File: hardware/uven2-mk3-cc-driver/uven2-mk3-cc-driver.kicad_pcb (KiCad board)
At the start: 2 copper layers, 80 x 32 mm, 23 parts, among them J1 Conn_01x03_Pin, J2 ADJ, J3 current_measurement, Q1 AO3401A, U2 LM3409HV

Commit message: ordered
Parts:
- removed D3: SS34, custom_lib:DIO_SS34
- added D1: SS54-HF, custom_lib:DIOM5025X220N, F.Cu at (126.0, 87.9)
- C1: value 3.3µF -> 16SVP3R3M; footprint Capacitor_SMD:C_Elec_5x5.4 -> custom_lib:CAP_16SVP3R3M
- L1: footprint Inductor_SMD:L_7.3x7.3_H3.5 -> custom_lib:HPC-8040NV-100M
- R1, R2, R3: footprint Resistor_SMD:R_0805_2012Metric_Pad1.20x1.40mm_HandSolder -> Resistor_SMD:R_0603_1608Metric_Pad0.98x0.95mm_HandSolder
- R4: footprint Resistor_SMD:R_0805_2012Metric_Pad1.20x1.40mm_HandSolder -> Resistor_SMD:R_2512_6332Metric_Pad1.40x3.35mm_HandSolder
- moved R1 5.09 mm to (115.1, 89.9), turned to 180 degrees
- moved C1 5.00 mm to (111.0, 103.4)
- moved R2 4.20 mm to (110.8, 89.9), turned to 180 degrees
- moved R4 3.85 mm to (118.5, 101.6)
- moved C2 1.10 mm to (108.2, 93.5), turned to 0 degrees
- turned L1 to 90 degrees
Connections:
- U2 pad 12: (no net) -> GND
- U2 pad 13: (no net) -> GND
- U2 pad 14: (no net) -> GND
- U2 pad 15: (no net) -> GND
- U2 pad 16: (no net) -> GND
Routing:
- net VCC: track 48.9 -> 34.6 mm
- net Net-(Q1-D): track 10.7 -> 13.0 mm
- net Net-(J2-Pin_2): track 15.6 -> 17.4 mm
- net GND: track 2.42 -> 1.49 mm, vias 6 -> 9
- net Net-(U2-COFF): track 43.5 -> 42.9 mm
- net Net-(U2-UVLO): track 6.93 -> 6.40 mm
- net Net-(J3-Pin_1): track 13.2 -> 12.7 mm
- added copper zone on F.Cu, net Net-(J3-Pin_1)
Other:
- board text added: "ADJ"
- board text added: "EN"
- board text added: "GND"
- board text added: "VCC"

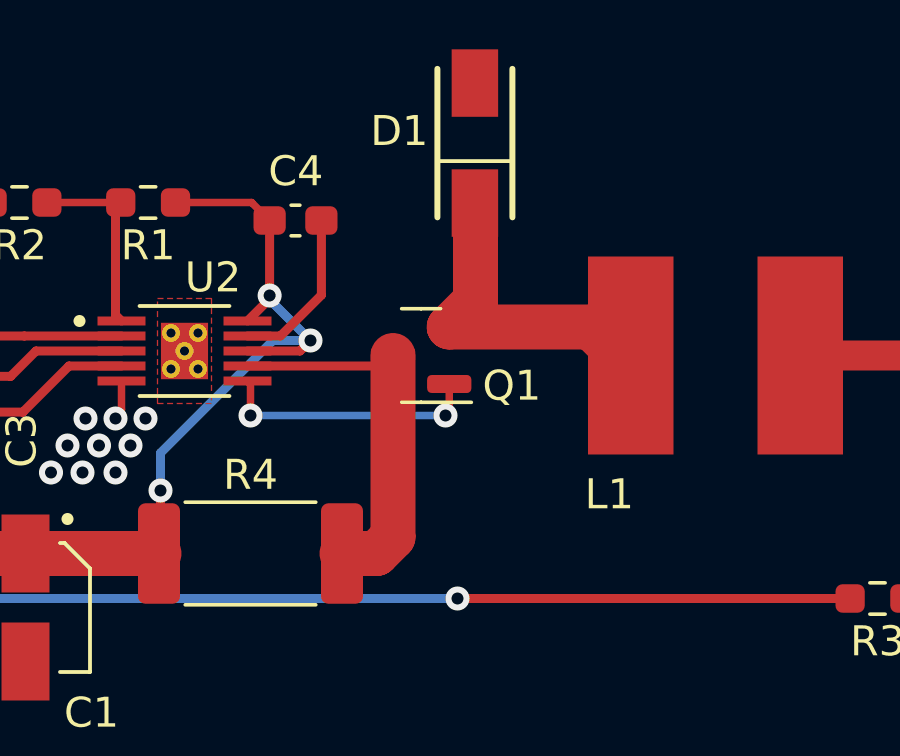
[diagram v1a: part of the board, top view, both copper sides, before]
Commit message: fix mosfet wrong orientation
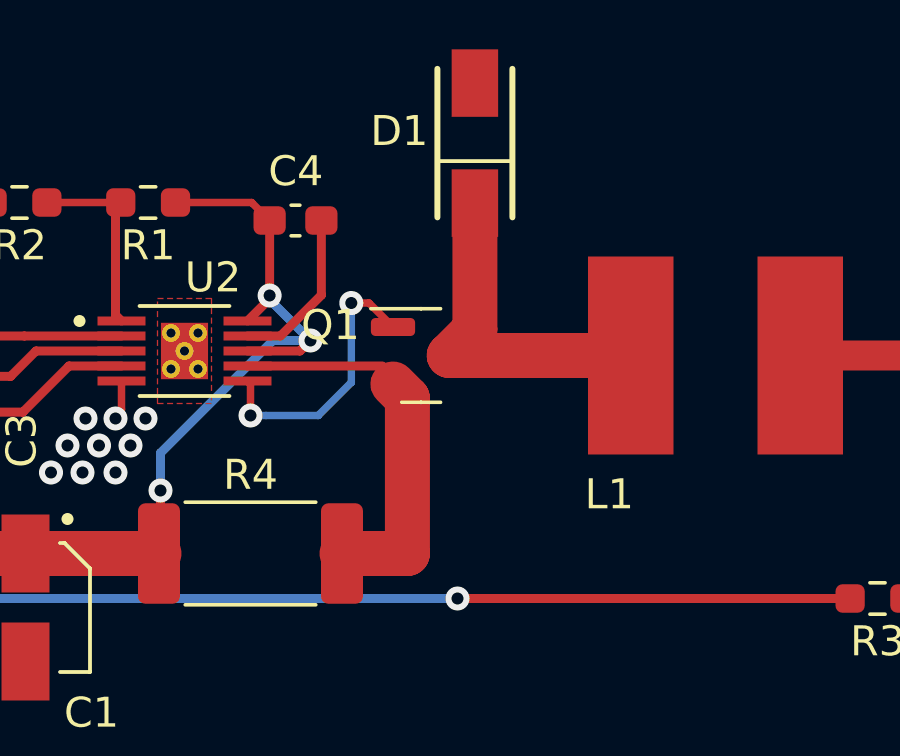
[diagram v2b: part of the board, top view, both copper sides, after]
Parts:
- turned Q1 to 0 degrees
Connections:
- D1 pad 1: Net-(Q1-S) -> Net-(Q1-D)
- L1 pad 1: Net-(Q1-S) -> Net-(Q1-D)
- R4 pad 2: Net-(Q1-D) -> Net-(Q1-S)
- U2 pad 12: GND -> (no net)
- U2 pad 13: GND -> (no net)
- U2 pad 14: GND -> (no net)
- U2 pad 15: GND -> (no net)
- U2 pad 16: GND -> (no net)
- U2 pad 7: Net-(Q1-D) -> Net-(Q1-S)
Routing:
- net Net-(Q1-S): track 10.6 -> 12.5 mm
- net Net-(Q1-D): track 13.0 -> 11.5 mm
- net Net-(Q1-G): track 8.78 -> 9.37 mm
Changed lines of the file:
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@@
       (stroke (width 0.1) (type solid)) (layer "F.Fab"))
     (pad "1" smd rect (at -2 0 90) (size 2.25 1.55) (layers "F.Cu" "F.Paste" "F.Mask")
-      (net 8 "Net-(Q1-S)") (pintype "bidirectional") (solder_mask_margin 0.102))
+      (net 10 "Net-(Q1-D)") (pintype "bidirectional") (solder_mask_margin 0.102))
     (pad "2" smd rect (at 2 0 90) (size 2.25 1.55) (layers "F.Cu" "F.Paste" "F.Mask")
       (net 2 "GND") (pintype "bidirectional") (solder_mask_margin 0.102))
@@
       (net 1 "VCC") (pintype "passive"))
     (pad "2" smd roundrect (at 3.05 0) (size 1.4 3.35) (layers "F.Cu" "F.Paste" "F.Mask") (roundrect_rratio 0.1785707143)
-      (net 10 "Net-(Q1-D)") (pintype "passive"))
+      (net 8 "Net-(Q1-S)") (pintype "passive"))
     (model "${KICAD6_3DMODEL_DIR}/Resistor_SMD.3dshapes/R_2512_6332Metric.wrl"
       (offset (xyz 0 0 0))
@@
       (net 9 "Net-(Q1-G)") (pinfunction "PGATE") (pintype "output"))
     (pad "7" smd rect (at 2.1 0.5) (size 1.6 0.3) (layers "F.Cu")
-      (net 10 "Net-(Q1-D)") (pinfunction "CSN") (pintype "input"))
+      (net 8 "Net-(Q1-S)") (pinfunction "CSN") (pintype "input"))
     (pad "8" smd rect (at 2.1 0) (size 1.6 0.3) (layers "F.Cu")
       (net 1 "VCC") (pinfunction "CSP") (pintype "input"))
@@
     (pad "11" smd rect (at 0 0) (size 1.57 1.88) (layers "F.Cu" "F.Paste" "F.Mask")
       (net 2 "GND") (pinfunction "PAD") (pintype "power_in") (solder_mask_margin 0.102))
-    (pad "12" thru_hole circle (at -0.45 -0.6) (size 0.6 0.6) (drill 0.3) (layers "*.Cu")
-      (net 2 "GND"))
-    (pad "13" thru_hole circle (at 0.45 -0.6) (size 0.6 0.6) (drill 0.3) (layers "*.Cu")
-      (net 2 "GND"))
-    (pad "14" thru_hole circle (at 0 0) (size 0.6 0.6) (drill 0.3) (layers "*.Cu")
-      (net 2 "GND"))
-    (pad "15" thru_hole circle (at -0.45 0.6) (size 0.6 0.6) (drill 0.3) (layers "*.Cu")
-      (net 2 "GND"))
-    (pad "16" thru_hole circle (at 0.45 0.6) (size 0.6 0.6) (drill 0.3) (layers "*.Cu")
-      (net 2 "GND"))
+    (pad "12" thru_hole circle (at -0.45 -0.6) (size 0.6 0.6) (drill 0.3) (layers "*.Cu"))
+    (pad "13" thru_hole circle (at 0.45 -0.6) (size 0.6 0.6) (drill 0.3) (layers "*.Cu"))
+    (pad "14" thru_hole circle (at 0 0) (size 0.6 0.6) (drill 0.3) (layers "*.Cu"))
+    (pad "15" thru_hole circle (at -0.45 0.6) (size 0.6 0.6) (drill 0.3) (layers "*.Cu"))
+    (pad "16" thru_hole circle (at 0.45 0.6) (size 0.6 0.6) (drill 0.3) (layers "*.Cu"))
   )
   (footprint "custom_lib:LED_SBT-10X-UV-A120-AH380-22" (layer "F.Cu")
@@
     )
     (pad "1" smd rect (at 0 -2.825 90) (size 6.6 2.85) (layers "F.Cu" "F.Paste" "F.Mask")
-      (net 8 "Net-(Q1-S)") (pintype "passive") (thermal_bridge_angle 45))
+      (net 10 "Net-(Q1-D)") (pintype "passive") (thermal_bridge_angle 45))
     (pad "2" smd rect (at 0 2.825 90) (size 6.6 2.85) (layers "F.Cu" "F.Paste" "F.Mask")
       (net 6 "Net-(J3-Pin_2)") (pintype "passive") (thermal_bridge_angle 45))
@@
   )
   (footprint "Package_TO_SOT_SMD:SOT-23" (layer "F.Cu")
-    (at 124.1875 95 180)
+    (at 124.1875 95)
     (descr "SOT, 3 Pin (https://www.jedec.org/system/files/docs/to-236h.pdf variant AB), generated with kicad-footprint-generator ipc_gullwing_generator.py")
     (tags "SOT TO_SOT_SMD")
@@
     (fp_line (start 0.65 1.45) (end -0.65 1.45)
       (stroke (width 0.1) (type solid)) (layer "F.Fab"))
-    (pad "1" smd roundrect (at -0.9375 -0.95 180) (size 1.475 0.6) (layers "F.Cu" "F.Paste" "F.Mask") (roundrect_rratio 0.25)
+    (pad "1" smd roundrect (at -0.9375 -0.95) (size 1.475 0.6) (layers "F.Cu" "F.Paste" "F.Mask") (roundrect_rratio 0.25)
       (net 9 "Net-(Q1-G)") (pinfunction "G") (pintype "input"))
-    (pad "2" smd roundrect (at -0.9375 0.95 180) (size 1.475 0.6) (layers "F.Cu" "F.Paste" "F.Mask") (roundrect_rratio 0.25)
+    (pad "2" smd roundrect (at -0.9375 0.95) (size 1.475 0.6) (layers "F.Cu" "F.Paste" "F.Mask") (roundrect_rratio 0.25)
       (net 8 "Net-(Q1-S)") (pinfunction "S") (pintype "passive"))
-    (pad "3" smd roundrect (at 0.9375 0 180) (size 1.475 0.6) (layers "F.Cu" "F.Paste" "F.Mask") (roundrect_rratio 0.25)
+    (pad "3" smd roundrect (at 0.9375 0) (size 1.475 0.6) (layers "F.Cu" "F.Paste" "F.Mask") (roundrect_rratio 0.25)
       (net 10 "Net-(Q1-D)") (pinfunction "D") (pintype "passive"))
     (model "${KICAD6_3DMODEL_DIR}/Package_TO_SOT_SMD.3dshapes/SOT-23.wrl"
@@
   (segment (start 143 95.1375) (end 148.5975 95.1375) (width 1) (layer "F.Cu") (net 6))
   (segment (start 153 97) (end 165.7 97) (width 1) (layer "F.Cu") (net 7))
-  (segment (start 129.85 94.05) (end 130.8 95) (width 1.5) (layer "F.Cu") (net 8))
-  (segment (start 126 89.9) (end 126 93.175) (width 1.5) (layer "F.Cu") (net 8))
-  (segment (start 126 93.175) (end 125.125 94.05) (width 1.5) (layer "F.Cu") (net 8))
-  (segment (start 125.125 94.05) (end 129.85 94.05) (width 1.5) (layer "F.Cu") (net 8))
+  (segment (start 123.73 96.43) (end 123.25 95.95) (width 1.5) (layer "F.Cu") (net 8))
+  (segment (start 121.55 101.6) (end 123.73 101.6) (width 1.5) (layer "F.Cu") (net 8))
+  (segment (start 122.9 95.35) (end 118.4 95.35) (width 0.3) (layer "F.Cu") (net 8))
+  (segment (start 123.73 101.6) (end 123.73 96.43) (width 1.5) (layer "F.Cu") (net 8))
   (segment (start 118.5 95.95) (end 118.425 95.875) (width 0.25) (layer "F.Cu") (net 9))
   (segment (start 118.425 95.875) (end 118.4 95.875) (width 0.25) (layer "F.Cu") (net 9))
   (segment (start 118.5 97) (end 118.5 95.95) (width 0.25) (layer "F.Cu") (net 9))
-  (segment (start 125.125 95.95) (end 125.125 96.875) (width 0.25) (layer "F.Cu") (net 9))
-  (segment (start 125.125 96.875) (end 125 97) (width 0.25) (layer "F.Cu") (net 9))
-  (via (at 125 97) (size 0.8) (drill 0.4) (layers "F.Cu" "B.Cu") (net 9))
+  (segment (start 121.86 93.25) (end 122.45 93.25) (width 0.25) (layer "F.Cu") (net 9))
+  (segment (start 122.45 93.25) (end 123.25 94.05) (width 0.25) (layer "F.Cu") (net 9))
   (via (at 118.5 97) (size 0.8) (drill 0.4) (layers "F.Cu" "B.Cu") (net 9))
-  (segment (start 125 97) (end 118.5 97) (width 0.25) (layer "B.Cu") (net 9))
-  (segment (start 123.25 95) (end 123.25 101.05) (width 1.5) (layer "F.Cu") (net 10))
-  (segment (start 123.25 101.05) (end 122.7 101.6) (width 1.5) (layer "F.Cu") (net 10))
-  (segment (start 122.7 101.6) (end 121.55 101.6) (width 1.5) (layer "F.Cu") (net 10))
-  (segment (start 122.9 95.35) (end 118.4 95.35) (width 0.3) (layer "F.Cu") (net 10))
-  (segment (start 123.25 95) (end 122.9 95.35) (width 0.25) (layer "F.Cu") (net 10))
+  (via (at 121.86 93.25) (size 0.8) (drill 0.4) (layers "F.Cu" "B.Cu") (net 9))
+  (segment (start 119.025305 97) (end 120.76 97) (width 0.25) (layer "B.Cu") (net 9))
+  (segment (start 118.5 97) (end 119.025305 97) (width 0.25) (layer "B.Cu") (net 9))
+  (segment (start 121.86 95.9) (end 121.86 93.25) (width 0.25) (layer "B.Cu") (net 9))
+  (segment (start 120.76 97) (end 121.86 95.9) (width 0.25) (layer "B.Cu") (net 9))
+  (segment (start 125.125 95) (end 131.175 95) (width 1.5) (layer "F.Cu") (net 10))
+  (segment (start 125.98 89.92) (end 125.98 94.145) (width 1.5) (layer "F.Cu") (net 10))
+  (segment (start 125.98 94.145) (end 125.125 95) (width 1.5) (layer "F.Cu") (net 10))
   (segment (start 114 90) (end 114 93.65) (width 0.3) (layer "F.Cu") (net 11))
   (segment (start 114 93.65) (end 114.2 93.85) (width 0.3) (layer "F.Cu") (net 11))
